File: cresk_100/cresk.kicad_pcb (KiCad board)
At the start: 2 copper layers, 100 x 100 mm, 52 parts, among them J1 8P8C, J2 8P8C, J3 Conn_01x05_Male, J4 Conn_01x05_Male, SW1 SW_Push, SW10 SW_Push, SW11 SW_Push, SW12 SW_Push, SW13 SW_Push, SW14 SW_Push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

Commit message: cresk_100: describe board dimension, staggers and more
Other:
- board text added: "Click here to select USB edge cuts."
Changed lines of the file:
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@@
     (effects (font (size 1 1) (thickness 0.15)) (justify left))
+  )
+  (gr_text "Click here to select\nUSB edge cuts." (at 48.2 49.19) (layer "Cmts.User")
+    (effects (font (size 1 1) (thickness 0.15)))
+  )
+  (dimension (type aligned) (layer "Dwgs.User")
+    (pts (xy 156.2 140.3) (xy 156.2 40.3))
+    (height 2)
+    (gr_text "100.0000 mm" (at 158.2 90.3 90) (layer "Dwgs.User")
+      (effects (font (size 2 2) (thickness 0.15)))
+    )
+    (format (units 3) (units_format 1) (precision 4))
+    (style (thickness 0.15) (arrow_length 1.27) (text_position_mode 1) (extension_height 0.58642) (extension_offset 0.5) keep_text_aligned)
+  )
+  (dimension (type aligned) (layer "Dwgs.User")
+    (pts (xy 153.2 50.3) (xy 123.2 50.3))
+    (height 22)
+    (gr_text "Maximum knob diameter 30.0000 mm" (at 138.2 26.15) (layer "Dwgs.User")
+      (effects (font (size 2 2) (thickness 0.15)))
+    )
+    (format (prefix "Maximum knob diameter ") (units 3) (units_format 1) (precision 4))
+    (style (thickness 0.15) (arrow_length 1.27) (text_position_mode 0) (extension_height 0.58642) (extension_offset 0.5) keep_text_aligned)
+  )
+  (dimension (type aligned) (layer "Dwgs.User")
+    (pts (xy 148.2 50.3) (xy 128.2 50.3))
+    (height 16)
+    (gr_text "20.0000 mm" (at 138.2 32.15) (layer "Dwgs.User")
+      (effects (font (size 2 2) (thickness 0.15)))
+    )
+    (format (units 3) (units_format 1) (precision 4))
+    (style (thickness 0.15) (arrow_length 1.27) (text_position_mode 0) (extension_height 0.58642) (extension_offset 0.5) keep_text_aligned)
+  )
+  (dimension (type aligned) (layer "Dwgs.User")
+    (pts (xy 148.2 148.3) (xy 48.2 148.3))
+    (height -2)
+    (gr_text "100.0000 mm" (at 98.2 150.3) (layer "Dwgs.User")
+      (effects (font (size 2 2) (thickness 0.15)))
+    )
+    (format (units 3) (units_format 1) (precision 4))
+    (style (thickness 0.15) (arrow_length 1.27) (text_position_mode 1) (extension_height 0.58642) (extension_offset 0.5) keep_text_aligned)
+  )
+  (dimension (type aligned) (layer "Edge.Cuts")
+    (pts (xy 65.5 66) (xy 65.5 78))
+    (height 1)
+    (gr_text "12.0000 mm" (at 61.5 78 90) (layer "Edge.Cuts")
+      (effects (font (size 2 2) (thickness 0.15)) (justify left))
+    )
+    (format (units 3) (units_format 1) (precision 4))
+    (style (thickness 0.1) (arrow_length 1.27) (text_position_mode 2) (extension_height 0.58642) (extension_offset 0.5) keep_text_aligned)
+  )
+  (dimension (type aligned) (layer "Edge.Cuts")
+    (pts (xy 103.5 137) (xy 111.9 137))
+    (height 6)
+    (gr_text "8.4000 mm" (at 107.7 146) (layer "Edge.Cuts")
+      (effects (font (size 2 2) (thickness 0.15)))
+    )
+    (format (units 3) (units_format 1) (precision 4))
+    (style (thickness 0.1) (arrow_length 1.27) (text_position_mode 2) (extension_height 0.58642) (extension_offset 0.5) keep_text_aligned)
+  )
+  (dimension (type aligned) (layer "Edge.Cuts")
+    (pts (xy 46.5 97) (xy 46.5 78))
+    (height -1)
+    (gr_text "19.0000 mm" (at 42.5 87.5 90) (layer "Edge.Cuts")
+      (effects (font (size 2 2) (thickness 0.15)))
+    )
+    (format (units 3) (units_format 1) (precision 4))
+    (style (thickness 0.1) (arrow_length 1.27) (text_position_mode 2) (extension_height 0.58642) (extension_offset 0.5) keep_text_aligned)
+  )
+  (dimension (type aligned) (layer "Edge.Cuts")
+    (pts (xy 84.5 61) (xy 84.5 66))
+    (height 0.999999)
+    (gr_text "5.0000 mm" (at 80.5 66 90) (layer "Edge.Cuts")
+      (effects (font (size 2 2) (thickness 0.15)) (justify left))
+    )
+    (format (units 3) (units_format 1) (precision 4))
+    (style (thickness 0.1) (arrow_length 1.27) (text_position_mode 2) (extension_height 0.58642) (extension_offset 0.5) keep_text_aligned)
+  )
+  (dimension (type aligned) (layer "Edge.Cuts")
+    (pts (xy 103.5 61) (xy 103.5 66))
+    (height -1)
+    (gr_text "5.0000 mm" (at 107.5 66 90) (layer "Edge.Cuts")
+      (effects (font (size 2 2) (thickness 0.15)) (justify left))
+    )
+    (format (units 3) (units_format 1) (precision 4))
+    (style (thickness 0.1) (arrow_length 1.27) (text_position_mode 2) (extension_height 0.58642) (extension_offset 0.5) keep_text_aligned)
   )
   (segment (start 68.04 80.58) (end 84.5 80.58) (width 1.27) (layer "B.Cu") (net 1))
@@
   (segment (start 86.554 58.842) (end 68.52 58.842) (width 0.508) (layer "B.Cu") (net 58))
   (segment (start 87.57 56.81) (end 86.554 58.842) (width 0.508) (layer "B.Cu") (net 58))
+  (group "" (id 50ce5aa2-15a2-4a99-8f2c-c4bde09ed6a8)
+    (members
+      a3c67dab-7d49-42ba-9f2b-53f4d61f5619
+      d6d20c9a-6a66-4a60-8842-8d311dbe5028
+    )
+  )
   (group "" (id d6d20c9a-6a66-4a60-8842-8d311dbe5028)
     (members

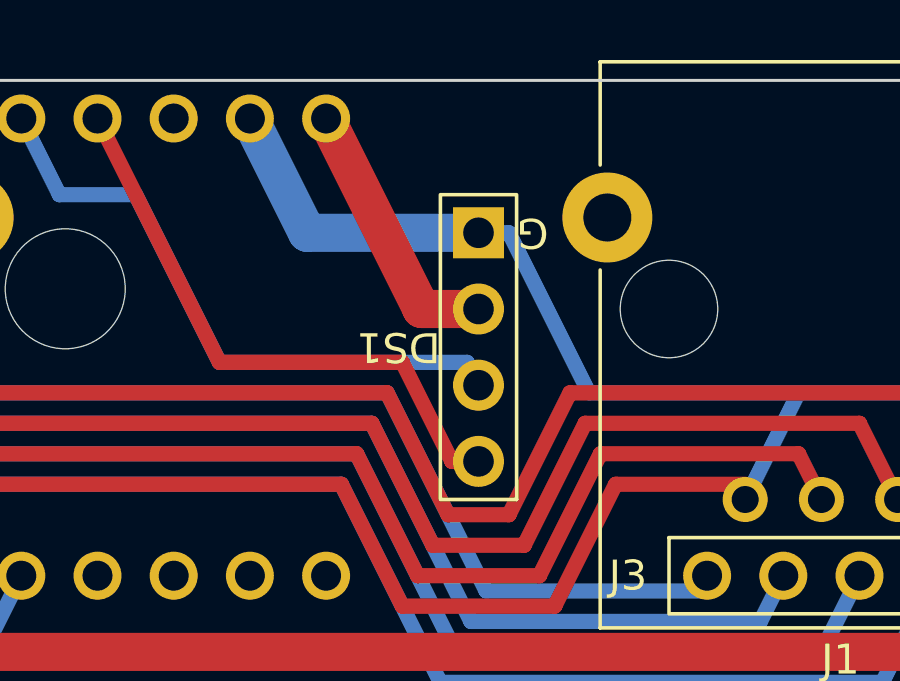
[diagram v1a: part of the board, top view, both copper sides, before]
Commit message: cresk_100: correct OLED footprint
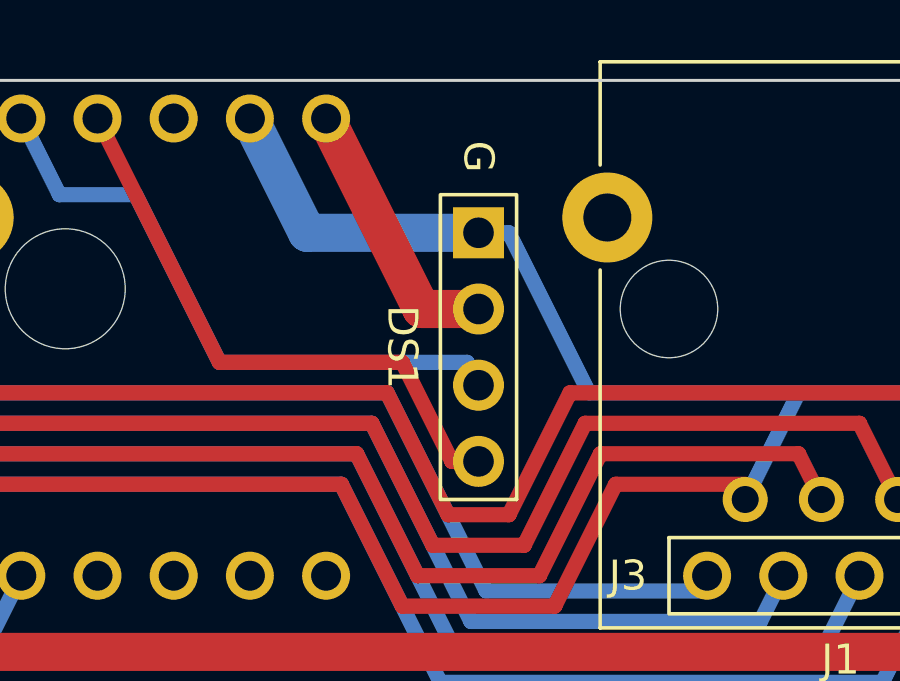
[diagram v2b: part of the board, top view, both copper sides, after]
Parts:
- turned DS1 to -90 degrees
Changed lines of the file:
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@@
   )
   (footprint "cresk:SSD1306_I2C" (layer "F.Cu")
-    (at 102.81 45.38 180)
+    (at 102.81 45.38 -90)
     (property "Sheetfile" "cresk.kicad_sch")
     (property "Sheetname" "")
     (attr through_hole)
-    (fp_text reference "DS1" (at 1.27 -3.81 180 unlocked) (layer "F.SilkS")
-      (effects (font (size 1 1) (thickness 0.15)) (justify left))
+    (fp_text reference "DS1" (at 3.81 2.54 -90 unlocked) (layer "F.SilkS")
+      (effects (font (size 1 1) (thickness 0.15)))
     )
-    (fp_text value "SSD1306_I2C" (at 1.27 -2.31 180 unlocked) (layer "F.Fab")
-      (effects (font (size 1 1) (thickness 0.15)) (justify left))
+    (fp_text value "SSD1306_I2C" (at 3.81 4.04 -90 unlocked) (layer "F.Fab")
+      (effects (font (size 1 1) (thickness 0.15)))
     )
-    (fp_text user "G" (at -1.27 0 180 unlocked) (layer "F.SilkS")
-      (effects (font (size 1 1) (thickness 0.15)) (justify right))
+    (fp_text user "G" (at -2.54 0 -90 unlocked) (layer "F.SilkS")
+      (effects (font (size 1 1) (thickness 0.15)))
     )
-    (fp_rect (start -1.27 -8.89) (end 1.27 1.27) (layer "F.SilkS") (width 0.12) (fill none))
-    (fp_rect (start -1.5 -9.81) (end 36.73 2.19) (layer "F.CrtYd") (width 0.05) (fill none))
-    (pad "1" thru_hole rect locked (at 0 0 180) (size 1.7 1.7) (drill 1.02) (layers *.Cu *.Mask)
+    (fp_rect (start 8.89 -1.27) (end -1.27 1.27) (layer "F.SilkS") (width 0.12) (fill none))
+    (fp_rect (start 9.81 -1.5) (end -2.19 36.73) (layer "F.CrtYd") (width 0.05) (fill none))
+    (pad "1" thru_hole rect (at 0 0 180) (size 1.7 1.7) (drill 1.02) (layers *.Cu *.Mask)
       (net 10 "GND") (pinfunction "GND") (pintype "power_in"))
-    (pad "2" thru_hole circle locked (at 0 -2.54 180) (size 1.7 1.7) (drill 1.02) (layers *.Cu *.Mask)
+    (pad "2" thru_hole circle (at 2.54 0 180) (size 1.7 1.7) (drill 1.02) (layers *.Cu *.Mask)
       (net 14 "VCC") (pinfunction "VCC") (pintype "power_in"))
-    (pad "3" thru_hole circle locked (at 0 -5.08 180) (size 1.7 1.7) (drill 1.02) (layers *.Cu *.Mask)
+    (pad "3" thru_hole circle (at 5.08 0 180) (size 1.7 1.7) (drill 1.02) (layers *.Cu *.Mask)
       (net 15 "SCL") (pinfunction "SCL") (pintype "bidirectional"))
-    (pad "4" thru_hole circle locked (at 0 -7.62 180) (size 1.7 1.7) (drill 1.02) (layers *.Cu *.Mask)
+    (pad "4" thru_hole circle (at 7.62 0 180) (size 1.7 1.7) (drill 1.02) (layers *.Cu *.Mask)
       (net 16 "SDA") (pinfunction "SDA") (pintype "bidirectional"))
   )
